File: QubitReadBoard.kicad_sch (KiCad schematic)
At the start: 0 parts

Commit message: Selected room temp amp
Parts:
- added U1: HMC8411LP2FE, CP_6_12_ADI, symbol HMC8411LP2FE:HMC8411LP2FE
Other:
- title: (none) -> Qubit Readout Board
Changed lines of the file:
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@@
 	(generator_version "10.0")
 	(paper "A4")
+	(title_block
+		(title "Qubit Readout Board")
+		(date "2026-08-18")
+	)
+	(symbol
+		(lib_id "HMC8411LP2FE:HMC8411LP2FE")
+		(at 48.26 101.6 0)
+		(unit 1)
+		(body_style 1)
+		(exclude_from_sim no)
+		(in_bom yes)
+		(on_board yes)
+		(in_pos_files yes)
+		(dnp no)
+		(fields_autoplaced yes)
+		(property "Reference" "U1"
+			(at 73.66 91.44 0)
+			(show_name no)
+			(do_not_autoplace no)
+			(effects
+				(font
+					(size 1.524 1.524)
+				)
+			)
+		)
+		(property "Value" "HMC8411LP2FE"
+			(at 73.66 93.98 0)
+			(show_name no)
+			(do_not_autoplace no)
+			(effects
+				(font
+					(size 1.524 1.524)
+				)
+			)
+		)
+		(property "Footprint" "CP_6_12_ADI"
+			(at 48.26 101.6 0)
+			(hide yes)
+			(show_name no)
+			(do_not_autoplace no)
+			(effects
+				(font
+					(size 1.27 1.27)
+					(italic yes)
+				)
+			)
+		)
+		(property "Datasheet" "https://www.analog.com/media/en/technical-documentation/data-sheets/HMC8411LP2FE.pdf"
+			(at 48.26 101.6 0)
+			(hide yes)
+			(show_name no)
+			(do_not_autoplace no)
+			(effects
+				(font
+					(size 1.27 1.27)
+					(italic yes)
+				)
+			)
+		)
+		(property "Description" ""
+			(at 48.26 101.6 0)
+			(hide yes)
+			(show_name no)
+			(do_not_autoplace no)
+			(effects
+				(font
+					(size 1.27 1.27)
+				)
+			)
+		)
+		(pin "2"
+		)
+		(pin "1"
+		)
+		(pin "5"
+		)
+		(pin "7"
+		)
+		(pin "4"
+		)
+		(pin "3"
+		)
+		(pin "6"
+		)
+		(instances
+			(project "QubitReadBoard"
+				(path "/56824d00-9c24-4fa5-a72f-e9b9506cb609"
+					(reference "U1")
+					(unit 1)
+				)
+			)
+		)
+	)
 	(sheet_instances
 		(path "/"

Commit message: Added mixer
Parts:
- added U3: LTC5552IUDB-TRPBF, UDB_12_ADI, symbol LTC5552:LTC5552IUDB-TRPBF
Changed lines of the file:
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@@
 	(title_block
 		(title "Qubit Readout Board")
-		(date "2026-08-18")
+		(date "2026-08-19")
 	)
 	(symbol
+		(lib_id "LTC5552:LTC5552IUDB-TRPBF")
+		(at 132.08 76.2 0)
+		(unit 1)
+		(body_style 1)
+		(exclude_from_sim no)
+		(in_bom yes)
+		(on_board yes)
+		(in_pos_files yes)
+		(dnp no)
+		(fields_autoplaced yes)
+		(property "Reference" "U3"
+			(at 152.4 66.04 0)
+			(show_name no)
+			(do_not_autoplace no)
+			(effects
+				(font
+					(size 1.524 1.524)
+				)
+			)
+		)
+		(property "Value" "LTC5552IUDB-TRPBF"
+			(at 152.4 68.58 0)
+			(show_name no)
+			(do_not_autoplace no)
+			(effects
+				(font
+					(size 1.524 1.524)
+				)
+			)
+		)
+		(property "Footprint" "UDB_12_ADI"
+			(at 132.08 76.2 0)
+			(hide yes)
+			(show_name no)
+			(do_not_autoplace no)
+			(effects
+				(font
+					(size 1.27 1.27)
+					(italic yes)
+				)
+			)
+		)
+		(property "Datasheet" "https://www.analog.com/media/en/technical-documentation/data-sheets/5552f.pdf"
+			(at 132.08 76.2 0)
+			(hide yes)
+			(show_name no)
+			(do_not_autoplace no)
+			(effects
+				(font
+					(size 1.27 1.27)
+					(italic yes)
+				)
+			)
+		)
+		(property "Description" ""
+			(at 132.08 76.2 0)
+			(hide yes)
+			(show_name no)
+			(do_not_autoplace no)
+			(effects
+				(font
+					(size 1.27 1.27)
+				)
+			)
+		)
+		(pin "9"
+		)
+		(pin "11"
+		)
+		(pin "8"
+		)
+		(pin "1"
+		)
+		(pin "7"
+		)
+		(pin "3"
+		)
+		(pin "4"
+		)
+		(pin "6"
+		)
+		(pin "2"
+		)
+		(pin "5"
+		)
+		(pin "10"
+		)
+		(pin "12"
+		)
+		(pin "13"
+		)
+		(instances
+			(project "QubitReadBoard"
+				(path "/56824d00-9c24-4fa5-a72f-e9b9506cb609"
+					(reference "U3")
+					(unit 1)
+				)
+			)
+		)
+	)
+	(symbol

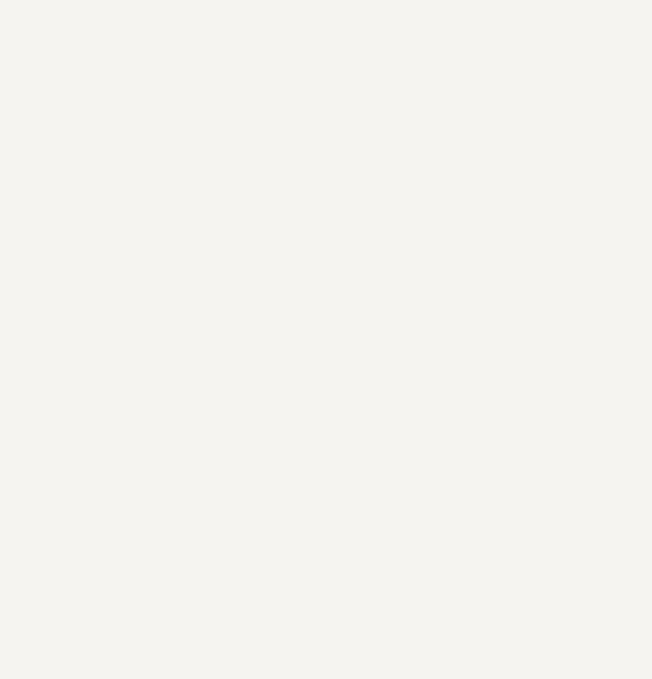
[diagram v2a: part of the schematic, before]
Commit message: Added AD9226 for ADC
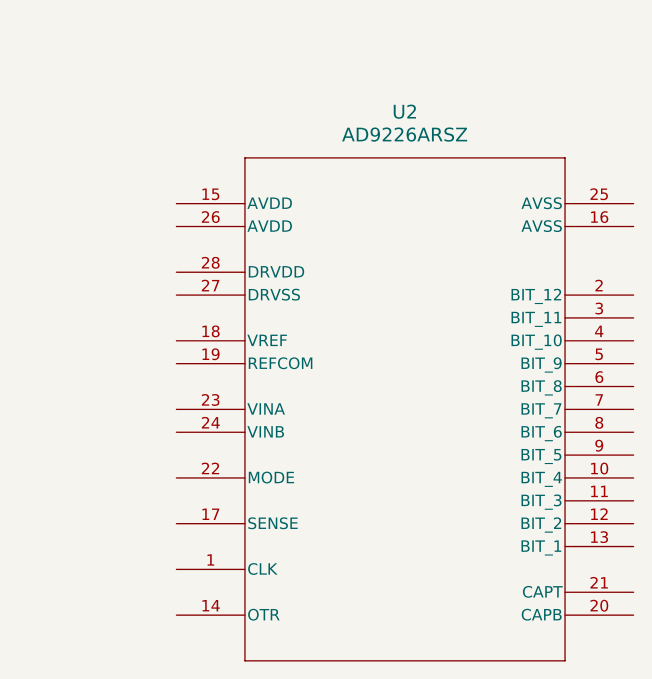
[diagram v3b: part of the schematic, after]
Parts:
- added U2: AD9226ARSZ, RS_28_ADI, symbol AD9226:AD9226ARSZ
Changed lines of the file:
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@@
 	(generator "eeschema")
 	(generator_version "10.0")
-	(paper "A4")
+	(paper "A3")
 	(title_block
 		(title "Qubit Readout Board")
@@
 					(unit 1)
 				)
+			)
+		)
+	)
+	(symbol
+		(lib_id "AD9226:AD9226ARSZ")
+		(at 212.09 85.09 0)
+		(unit 1)
+		(body_style 1)
+		(exclude_from_sim no)
+		(in_bom yes)
+		(on_board yes)
+		(in_pos_files yes)
+		(dnp no)
+		(fields_autoplaced yes)
+		(property "Reference" "U2"
+			(at 237.49 74.93 0)
+			(show_name no)
+			(do_not_autoplace no)
+			(effects
+				(font
+					(size 1.524 1.524)
+				)
+			)
+		)
+		(property "Value" "AD9226ARSZ"
+			(at 237.49 77.47 0)
+			(show_name no)
+			(do_not_autoplace no)
+			(effects
+				(font
+					(size 1.524 1.524)
+				)
+			)
+		)
+		(property "Footprint" "RS_28_ADI"
+			(at 212.09 85.09 0)
+			(hide yes)
+			(show_name no)
+			(do_not_autoplace no)
+			(effects
+				(font
+					(size 1.27 1.27)
+					(italic yes)
+				)
+			)
+		)
+		(property "Datasheet" "https://www.analog.com/media/en/technical-documentation/data-sheets/AD9226.pdf"
+			(at 212.09 85.09 0)
+			(hide yes)
+			(show_name no)
+			(do_not_autoplace no)
+			(effects
+				(font
+					(size 1.27 1.27)
+					(italic yes)
+				)
+			)
+		)
+		(property "Description" ""
+			(at 212.09 85.09 0)
+			(hide yes)
+			(show_name no)
+			(do_not_autoplace no)
+			(effects
+				(font
+					(size 1.27 1.27)
+				)
+			)
+		)
+		(pin "1"
+		)
+		(pin "11"
+		)
+		(pin "2"
+		)
+		(pin "4"
+		)
+		(pin "15"
+		)
+		(pin "17"
+		)
+		(pin "20"
+		)
+		(pin "7"
+		)
+		(pin "19"
+		)
+		(pin "3"
+		)
+		(pin "5"
+		)
+		(pin "6"
+		)
+		(pin "8"
+		)
+		(pin "9"
+		)
+		(pin "10"
+		)
+		(pin "12"
+		)
+		(pin "13"
+		)
+		(pin "14"
+		)
+		(pin "16"
+		)
+		(pin "18"
+		)
+		(pin "24"
+		)
+		(pin "25"
+		)
+		(pin "22"
+		)
+		(pin "21"
+		)
+		(pin "26"
+		)
+		(pin "27"
+		)
+		(pin "28"
+		)
+		(pin "23"
+		)
+		(instances
+			(project "QubitReadBoard"
+				(path "/56824d00-9c24-4fa5-a72f-e9b9506cb609"
+					(reference "U2")
+					(unit 1)
+				)

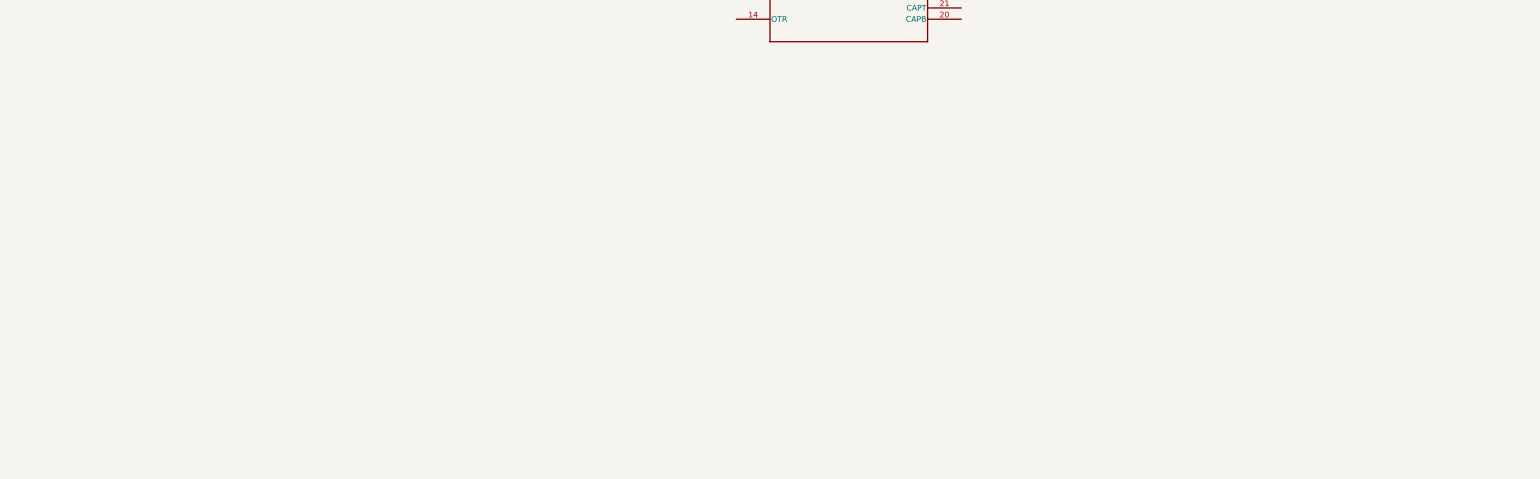
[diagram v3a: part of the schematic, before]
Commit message: Picked IF amp and PLL
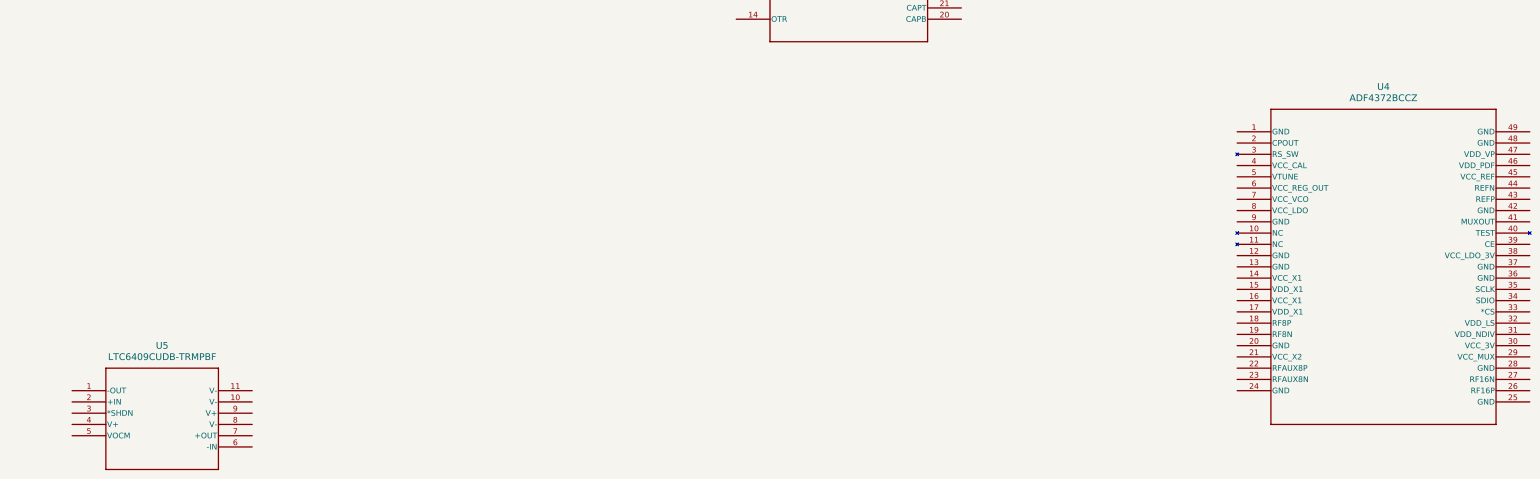
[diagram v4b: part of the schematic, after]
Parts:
- added U4: ADF4372BCCZ, CC-48-4_ADI, symbol ADF4372:ADF4372BCCZ
- added U5: LTC6409CUDB-TRMPBF, QFN-10_UDB_LIT, symbol LTC6409:LTC6409CUDB-TRMPBF

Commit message: Added LNA circuit
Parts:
- added C100, C101, C102, C103: 100nF, symbol Device:C
- added C104: 10pF, symbol Device:C
- added J1: SMA, symbol Connector_Generic_Shielded:Conn_01x01_Shielded
- added L100: 590nH, symbol Device:L
- added L101: 33nH, symbol Device:L
- added R100: 43R, symbol Device:R
- added R101: 1.1k, symbol Device:R
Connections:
- net at U1.1 (RBIAS): now also R101.2
- net at U1.2 (RFIN): now also C100.2, L100.1
- net at U1.5 (RFOUT/VDD): now also C102.1, L101.2
- net GND: now reaches U1.6 (GND)
- net GND: now also U1.7 (EPAD), C101.2, C103.2, C104.2, J1.SH (Shield)
- new net: C101.1, R100.2
- new net: L100.2, R100.1
- new net +5V: C103.1, C104.1, L101.1, R101.1
- new net LNA_FROUT: C102.2
- new net LNA_RFIN: C100.1
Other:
- note added: "LNA"
- moved on the sheet: U1, U2, U3, U4, U5
